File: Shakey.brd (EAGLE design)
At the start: 148.3 x 60.9 mm, 84 parts, among them CN1 CONN_USB-4UCON-11071, CN2 ISP, U1 ATMEGA32U4-AU, U2 ICM-20689, U3 AP2210K-3.3TRG1, Y1 16Mhz

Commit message: 90 percent parts placed
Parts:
- removed EARTH6: (no value), SixthLogic:MA01-1-ALLIGATOR-3MM
- removed LED1, LED2, LED3, LED4, LED5, LED6: GREEN, SixthLogic:LED-1206-LTST-BOTTOM
- removed R15, R16: 22M, rcl:R0603
- removed U$6: LM75AD, SixthLogic:SOT96-1
- added LED_CLICK, LED_DOWN, LED_LEFT, LED_RIGHT, LED_SPACE, LED_UP: GREEN, SixthLogic:LED-1206-LTST-BOTTOM
- added U4: LM75AD, SixthLogic:SOT96-1
- LED7, LED8, LED9: device led:CHIPLED_0603 -> SixthLogic:LED-1206-LTST-BOTTOM
- moved MOUSE-DOWN 143.4 mm to (57.4, -14.1), flipped to the bottom
- moved C9 135.8 mm to (71.8, 40.4), flipped to the bottom
- moved R20 134.6 mm to (57.4, -10.0), flipped to the bottom
- moved MOUSE-RIGHT-CLICK 124.5 mm to (58.5, 0.00), flipped to the bottom, turned to 270 degrees
- moved MOUSE-UP 115.3 mm to (27.0, -14.1), flipped to the bottom
- moved MOUSE-RIGHT 108.8 mm to (57.4, 14.0), flipped to the bottom
- moved SPACE 106.6 mm to (42.2, -15.2), flipped to the bottom, turned to 270 degrees
- moved R19 102.6 mm to (27.0, -10.0), flipped to the bottom
- moved R23 99.8 mm to (62.0, 0.00), flipped to the bottom, turned to 270 degrees
- moved EARTH4 93.6 mm to (0.00, -11.7), flipped to the bottom, turned to 270 degrees
- moved C8 92.9 mm to (50.2, 63.2), flipped to the bottom
- moved EARTH3 92.4 mm to (6.60, -12.2), flipped to the bottom, turned to 270 degrees
- moved EARTH2 91.6 mm to (13.2, -13.2), flipped to the bottom, turned to 270 degrees
- moved C10 89.6 mm to (6.00, -3.00), flipped to the bottom, turned to 90 degrees
- moved R8 87.7 mm to (46.0, -15.2), flipped to the bottom, turned to 90 degrees
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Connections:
- net 3.3V: now also C10.2, U4.8
- net GND: now also U4.4, U4.5, U4.6, U4.7; no longer EARTH6.1@0, EARTH6.1@1, U$6.4, U$6.5, U$6.6, U$6.7
- net N$11: now also LED_CLICK.C, LED_RIGHT.A, LED_SPACE.A, LED_UP.C; no longer LED3.C, LED4.A, LED5.C, LED6.A
- net N$12: now also LED_DOWN.C, LED_LEFT.A, LED_RIGHT.C, LED_UP.A; no longer LED1.C, LED2.A, LED5.A, LED6.C
- net N$4: now also LED_CLICK.A, LED_DOWN.A, LED_LEFT.C, LED_SPACE.C; no longer LED1.A, LED2.C, LED3.A, LED4.C
- net SCL_HV: no longer U$6.2
- net SCL_LV: now also U4.2
- net SDA_HV: no longer U$6.1
- net SDA_LV: now also U4.1
- net VCC: no longer C10.2, R15.2, R16.2, U$6.8
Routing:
- added copper zone on layer 1, net D6
- added copper zone on layer 1, net N$14
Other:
- board size 148.3 x 60.9 mm -> 146.4 x 62.1 mm

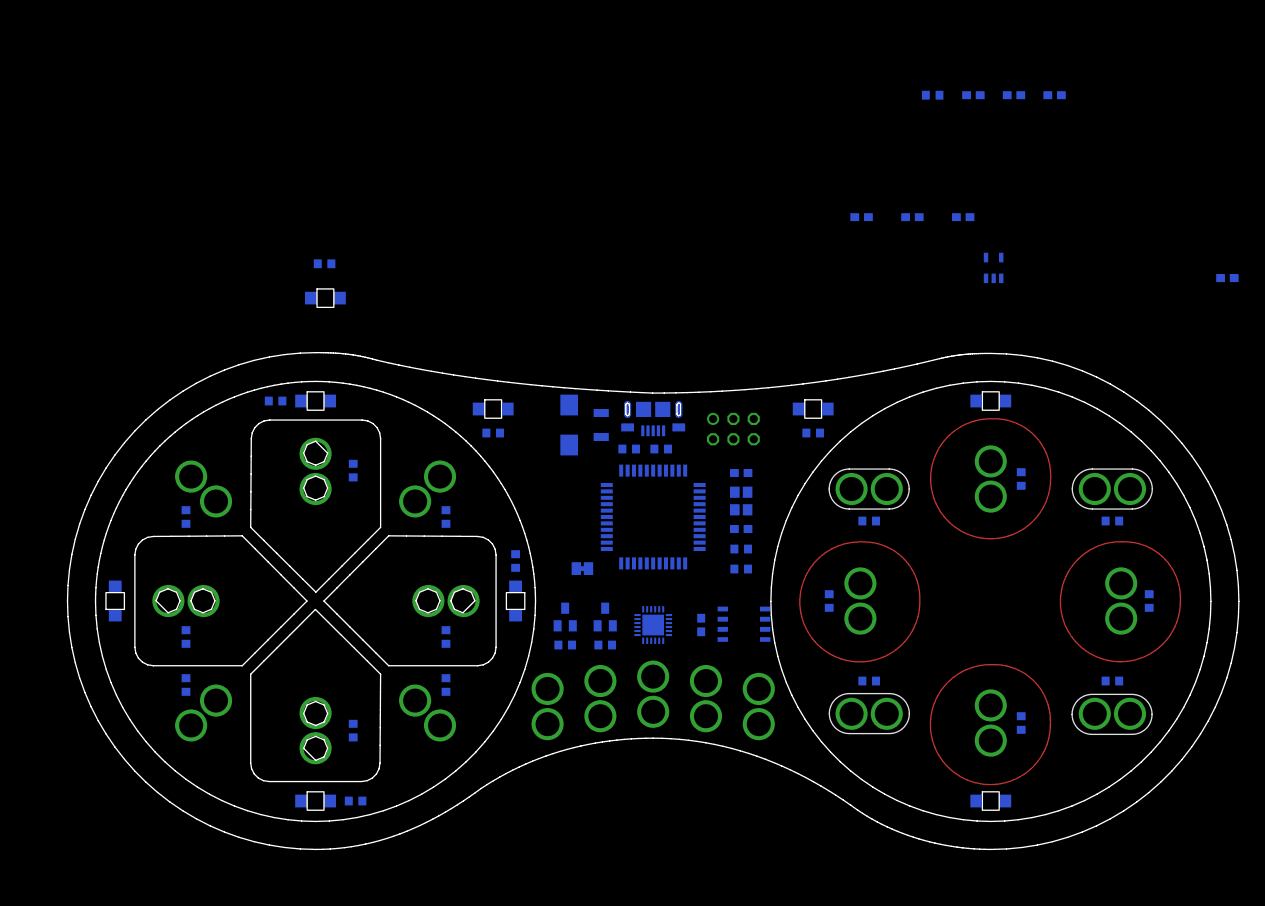
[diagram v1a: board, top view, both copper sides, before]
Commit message: completed arranging parts
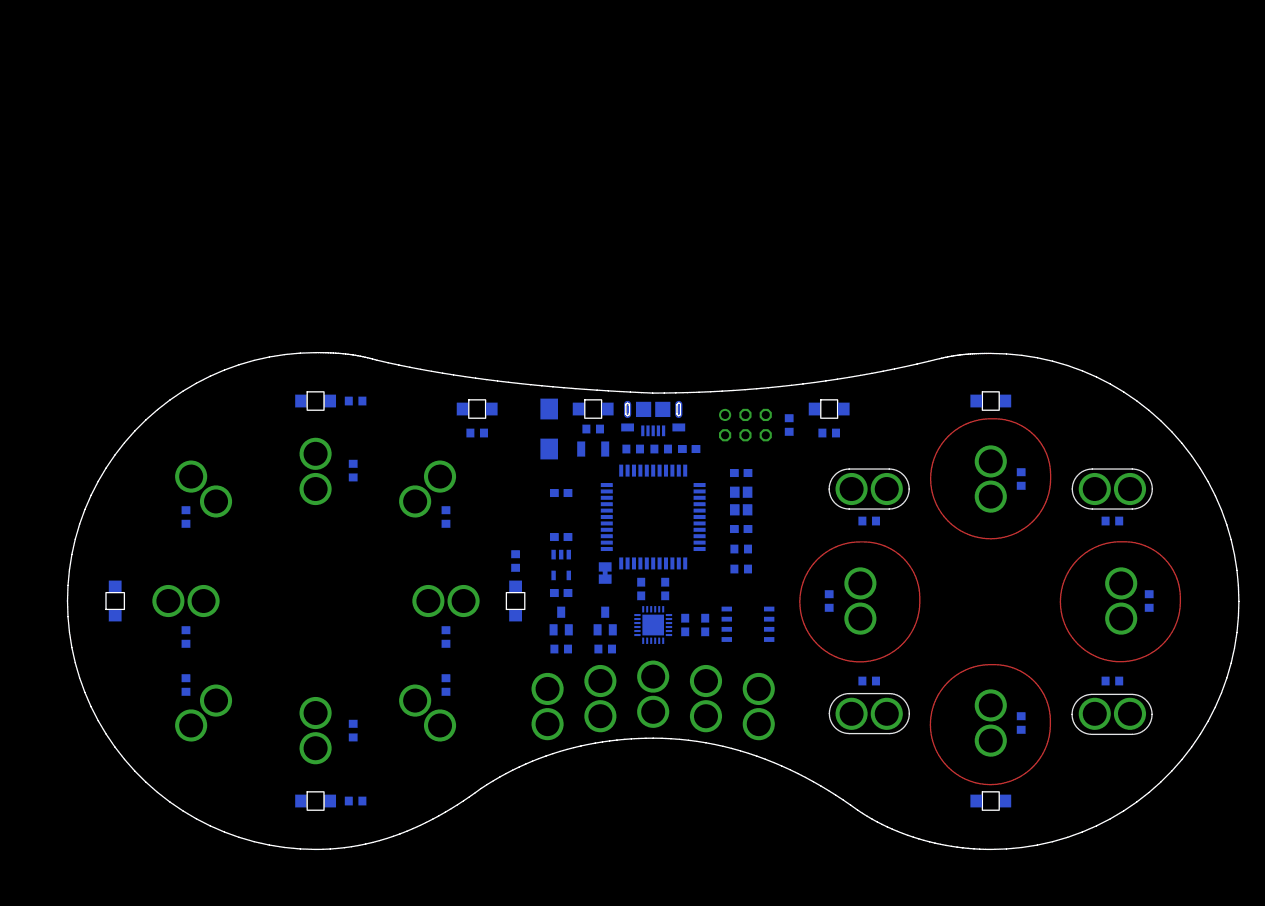
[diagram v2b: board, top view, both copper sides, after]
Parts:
- moved C5 84.1 mm to (-11.5, 1.00)
- moved C8 82.8 mm to (-11.5, 8.00)
- moved C9 80.5 mm to (4.00, -3.00), turned to 270 degrees
- moved U3 65.6 mm to (-11.5, 4.50), turned to 180 degrees
- moved C7 61.5 mm to (-1.50, 1.50), turned to 90 degrees
- moved C3 56.7 mm to (4.50, 19.0)
- moved C6 55.8 mm to (1.50, 1.50), turned to 90 degrees
- moved C4 51.0 mm to (-11.5, 13.5), turned to 180 degrees
- moved R3 45.0 mm to (17.0, 22.0), turned to 270 degrees
- moved R27 39.4 mm to (-7.50, 21.5)
- moved LED9 36.2 mm to (-7.50, 24.0)
- moved R12 10.0 mm to (-37.2, 25.0), turned to 0 degrees
- moved F1 3.16 mm to (-7.50, 19.0), turned to 0 degrees
- moved SJ1 2.90 mm to (-6.00, 3.50), turned to 90 degrees
- moved PC1 2.55 mm to (-13.0, 21.5)
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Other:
- outline, holes or cut-outs redrawn

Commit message: 50 percent tracks done
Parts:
- moved R29 25.6 mm to (13.2, 0.50)
- moved TR2 25.5 mm to (13.2, 3.75)
- moved R28 16.6 mm to (9.25, 0.50)
- moved TR1 16.5 mm to (9.25, 3.75)
- moved C7 6.82 mm to (-2.50, -5.25)
- moved C6 6.79 mm to (2.25, -5.25)
- moved R25 5.20 mm to (26.2, 24.0), turned to 90 degrees
- moved R26 5.06 mm to (-17.8, 23.8), turned to 90 degrees
- moved C9 4.59 mm to (0.00, -5.25), turned to 90 degrees
- moved R30 3.64 mm to (10.0, 7.50), turned to 90 degrees
- moved C5 3.00 mm to (-11.5, 4.00)
- moved C8 3.00 mm to (-11.5, 11.0)
- moved U3 3.00 mm to (-11.5, 7.50)
- moved U2 2.50 mm to (0.00, -0.50)
- moved C1 2.00 mm to (11.0, 11.0), turned to 180 degrees
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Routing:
- net VCC: track 0.00 -> 364.5 mm, vias 0 -> 2
- net N$4: track 0.00 -> 123.2 mm
- net N$12: track 0.00 -> 122.3 mm
- net N$11: track 0.00 -> 119.5 mm
- net 3.3V: track 0.00 -> 59.8 mm, vias 0 -> 3
- net GND: track 0.00 -> 50.1 mm
- net SCL_LV: track 0.00 -> 25.6 mm, vias 0 -> 2
- net D15: track 0.00 -> 23.4 mm, vias 0 -> 1
- net !RESET!: track 0.00 -> 19.2 mm
- net SDA_LV: track 0.00 -> 15.6 mm
- net D16: track 0.00 -> 13.8 mm
- net SCL_HV: track 0.00 -> 13.8 mm
- net A4: track 0.00 -> 11.5 mm, vias 0 -> 1
- net A2: track 0.00 -> 11.4 mm, vias 0 -> 1
- net D14: track 0.00 -> 11.1 mm
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- added copper zone on layer 1, net A0
- added copper zone on layer 1, net A1
- added copper zone on layer 1, net D12
- added copper zone on layer 1, net D13
- added copper zone on layer 1, net D15
- added copper zone on layer 1, net D7
- added copper zone on layer 1, net D8
- removed copper zone on layer 1, net N$14

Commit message: finished tracks
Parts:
- moved R2 1.00 mm to (0.00, 19.0)
- moved R1 0.75 mm to (-3.25, 19.0), turned to 180 degrees
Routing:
- net N$4: track 123.2 -> 230.4 mm, vias 0 -> 2
- net VCC: track 364.5 -> 467.1 mm, vias 2 -> 9
- net A4: track 11.5 -> 108.5 mm
- net D13: track 6.36 -> 99.9 mm, vias 1 -> 3
- net N$11: track 119.5 -> 210.8 mm, vias 0 -> 2
- net D4: track 8.87 -> 93.3 mm, vias 0 -> 2
- net A1: track 1.50 -> 78.6 mm, vias 1 -> 4
- net A2: track 11.4 -> 85.4 mm, vias 1 -> 3
- net D7: track 4.43 -> 76.6 mm, vias 0 -> 2
- net D5: track 10.1 -> 82.0 mm, vias 1 -> 2
- net D8: track 7.01 -> 71.6 mm
- net D6: track 4.36 -> 68.6 mm, vias 0 -> 3
- net D12: track 5.22 -> 63.9 mm, vias 0 -> 3
- net D1: track 8.91 -> 66.5 mm, vias 0 -> 1
- net GND: track 50.1 -> 103.2 mm, vias 0 -> 13
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- added copper zone on layer 16, net GND
